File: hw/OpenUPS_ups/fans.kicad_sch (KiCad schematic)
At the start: 9 parts, among them J601 0022053031, J602 0022053031, Q601 2N7002, Q602 2N7002

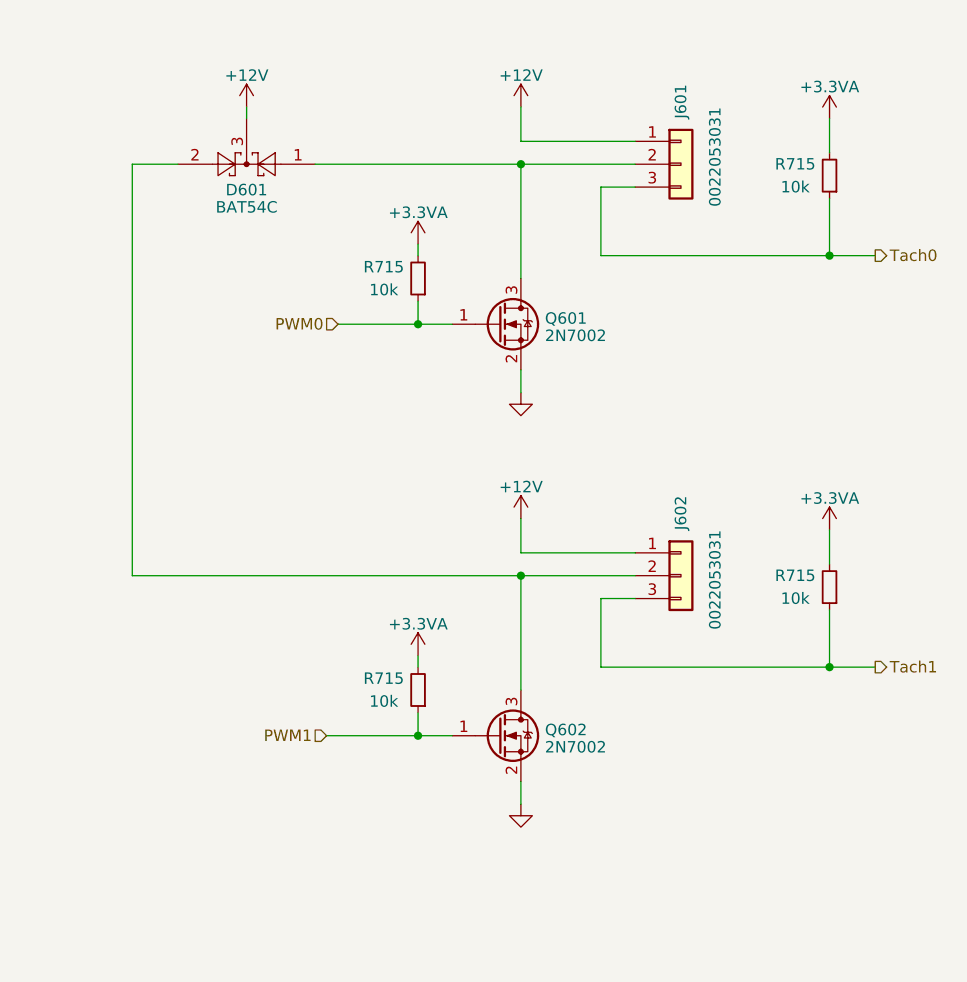
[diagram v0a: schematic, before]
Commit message: Added ports and fuses
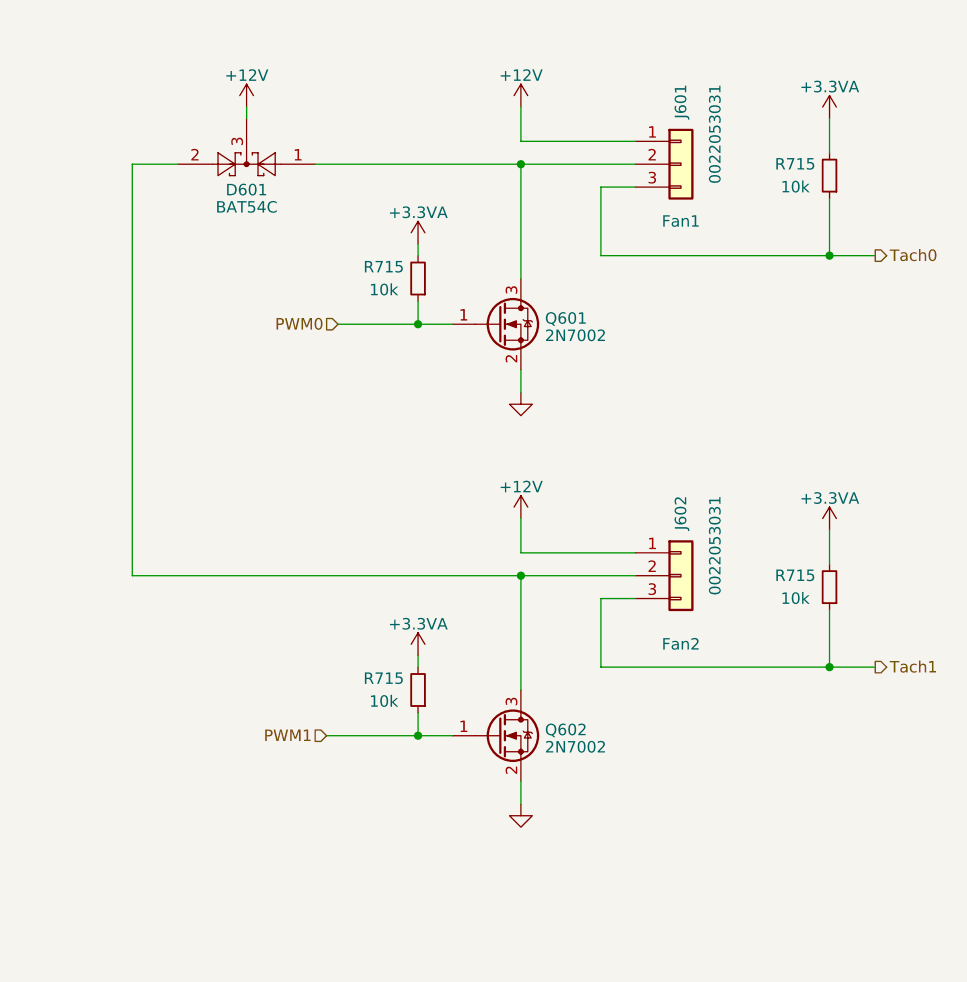
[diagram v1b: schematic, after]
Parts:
- J601: Label (none) -> Fan1
- J602: Label (none) -> Fan2
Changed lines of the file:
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@@
       (effects (font (size 1.27 1.27)) (justify right))
     )
-    (property "Value" "0022053031" (at 114.3 78.74 90)
+    (property "Value" "0022053031" (at 114.3 76.2 90)
       (effects (font (size 1.27 1.27)) (justify right))
     )
@@
     (property "Datasheet" "https://www.molex.com/pdm_docs/sd/022053031_sd.pdf" (at 110.49 85.09 0)
       (effects (font (size 1.27 1.27)) hide)
+    )
+    (property "Label" "Fan1" (at 110.49 91.44 0)
+      (effects (font (size 1.27 1.27)))
     )
     (pin "1")
@@
       (effects (font (size 1.27 1.27)) (justify right))
     )
-    (property "Value" "0022053031" (at 114.3 125.73 90)
+    (property "Value" "0022053031" (at 114.3 121.92 90)
       (effects (font (size 1.27 1.27)) (justify right))
     )
@@
       (effects (font (size 1.27 1.27)) hide)
     )
-    (pin "1")
+    (property "Label" "Fan2" (at 110.49 138.43 0)
+      (effects (font (size 1.27 1.27)))
+    )
+    (pin "1")

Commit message: Initial placement effort
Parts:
- renumbered D601 to D701, J601 to J701, J602 to J702, Q601 to Q701, Q602 to Q702
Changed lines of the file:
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@@
         )
         (path "/f77faec3-eac4-47f3-a2de-ec4a039f4502/4e3a8bef-51a9-4147-914d-0da741181736"
-          (reference "#PWR0608") (unit 1)
+          (reference "#PWR0702") (unit 1)
         )
       )
@@
         )
         (path "/f77faec3-eac4-47f3-a2de-ec4a039f4502/4e3a8bef-51a9-4147-914d-0da741181736"
-          (reference "#PWR0604") (unit 1)
+          (reference "#PWR0704") (unit 1)
         )
       )
@@
   (symbol (lib_id "Transistor_FET:2N7002") (at 90.17 102.87 0) (unit 1)
     (in_bom yes) (on_board yes) (dnp no) (fields_autoplaced)
-    (property "Reference" "Q601" (at 95.377 102.2263 0)
+    (property "Reference" "Q701" (at 95.377 102.2263 0)
       (effects (font (size 1.27 1.27)) (justify left))
     )
@@
       (project "OpenUPS_ups"
         (path "/f77faec3-eac4-47f3-a2de-ec4a039f4502/4e3a8bef-51a9-4147-914d-0da741181736"
-          (reference "Q601") (unit 1)
+          (reference "Q701") (unit 1)
         )
       )
@@
         )
         (path "/f77faec3-eac4-47f3-a2de-ec4a039f4502/4e3a8bef-51a9-4147-914d-0da741181736"
-          (reference "#PWR0607") (unit 1)
+          (reference "#PWR0708") (unit 1)
         )
       )
@@
         )
         (path "/f77faec3-eac4-47f3-a2de-ec4a039f4502/4e3a8bef-51a9-4147-914d-0da741181736"
-          (reference "#PWR0601") (unit 1)
+          (reference "#PWR0705") (unit 1)
         )
       )
@@
   (symbol (lib_id "Connector_Generic:Conn_01x03") (at 110.49 85.09 0) (unit 1)
     (in_bom yes) (on_board yes) (dnp no)
-    (property "Reference" "J601" (at 110.49 76.2 90)
+    (property "Reference" "J701" (at 110.49 76.2 90)
       (effects (font (size 1.27 1.27)) (justify right))
     )
@@
       (project "OpenUPS_ups"
         (path "/f77faec3-eac4-47f3-a2de-ec4a039f4502/4e3a8bef-51a9-4147-914d-0da741181736"
-          (reference "J601") (unit 1)
+          (reference "J701") (unit 1)
         )
       )
@@
         )
         (path "/f77faec3-eac4-47f3-a2de-ec4a039f4502/4e3a8bef-51a9-4147-914d-0da741181736"
-          (reference "#PWR0603") (unit 1)
+          (reference "#PWR0701") (unit 1)
         )
       )
@@
         )
         (path "/f77faec3-eac4-47f3-a2de-ec4a039f4502/4e3a8bef-51a9-4147-914d-0da741181736"
-          (reference "#PWR0605") (unit 1)
+          (reference "#PWR0706") (unit 1)
         )
       )
@@
         )
         (path "/f77faec3-eac4-47f3-a2de-ec4a039f4502/4e3a8bef-51a9-4147-914d-0da741181736"
-          (reference "#PWR0609") (unit 1)
+          (reference "#PWR0703") (unit 1)
         )
       )
@@
   (symbol (lib_id "Transistor_FET:2N7002") (at 90.17 148.59 0) (unit 1)
     (in_bom yes) (on_board yes) (dnp no) (fields_autoplaced)
-    (property "Reference" "Q602" (at 95.377 147.9463 0)
+    (property "Reference" "Q702" (at 95.377 147.9463 0)
       (effects (font (size 1.27 1.27)) (justify left))
     )
@@
       (project "OpenUPS_ups"
         (path "/f77faec3-eac4-47f3-a2de-ec4a039f4502/4e3a8bef-51a9-4147-914d-0da741181736"
-          (reference "Q602") (unit 1)
+          (reference "Q702") (unit 1)
         )
       )
@@
         )
         (path "/f77faec3-eac4-47f3-a2de-ec4a039f4502/4e3a8bef-51a9-4147-914d-0da741181736"
-          (reference "#PWR0602") (unit 1)
+          (reference "#PWR0709") (unit 1)
         )
       )
@@
   (symbol (lib_id "Diode:BAT54C") (at 62.23 85.09 180) (unit 1)
     (in_bom yes) (on_board yes) (dnp no) (fields_autoplaced)
-    (property "Reference" "D601" (at 62.23 87.9555 0)
+    (property "Reference" "D701" (at 62.23 87.9555 0)
       (effects (font (size 1.27 1.27)))
     )
@@
       (project "OpenUPS_ups"
         (path "/f77faec3-eac4-47f3-a2de-ec4a039f4502/4e3a8bef-51a9-4147-914d-0da741181736"
-          (reference "D601") (unit 1)
+          (reference "D701") (unit 1)
         )
       )
@@
         )
         (path "/f77faec3-eac4-47f3-a2de-ec4a039f4502/4e3a8bef-51a9-4147-914d-0da741181736"
-          (reference "R513") (unit 1)
+          (reference "R701") (unit 1)
         )
       )
@@
         )
         (path "/f77faec3-eac4-47f3-a2de-ec4a039f4502/4e3a8bef-51a9-4147-914d-0da741181736"
-          (reference "#PWR0606") (unit 1)
+          (reference "#PWR0707") (unit 1)
         )
       )
@@
         )
         (path "/f77faec3-eac4-47f3-a2de-ec4a039f4502/4e3a8bef-51a9-4147-914d-0da741181736"
-          (reference "R601") (unit 1)
+          (reference "R703") (unit 1)
         )
       )
@@
   (symbol (lib_id "Connector_Generic:Conn_01x03") (at 110.49 130.81 0) (unit 1)
     (in_bom yes) (on_board yes) (dnp no)
-    (property "Reference" "J602" (at 110.49 121.92 90)
+    (property "Reference" "J702" (at 110.49 121.92 90)
       (effects (font (size 1.27 1.27)) (justify right))
     )
@@
       (project "OpenUPS_ups"
         (path "/f77faec3-eac4-47f3-a2de-ec4a039f4502/4e3a8bef-51a9-4147-914d-0da741181736"
-          (reference "J602") (unit 1)
+          (reference "J702") (unit 1)
         )
       )
@@
         )
         (path "/f77faec3-eac4-47f3-a2de-ec4a039f4502/4e3a8bef-51a9-4147-914d-0da741181736"
-          (reference "R602") (unit 1)
+          (reference "R704") (unit 1)
         )
       )
@@
         )
         (path "/f77faec3-eac4-47f3-a2de-ec4a039f4502/4e3a8bef-51a9-4147-914d-0da741181736"
-          (reference "R514") (unit 1)
-        )
-      )
+          (reference "R702") (unit 1)
+        )
+      )

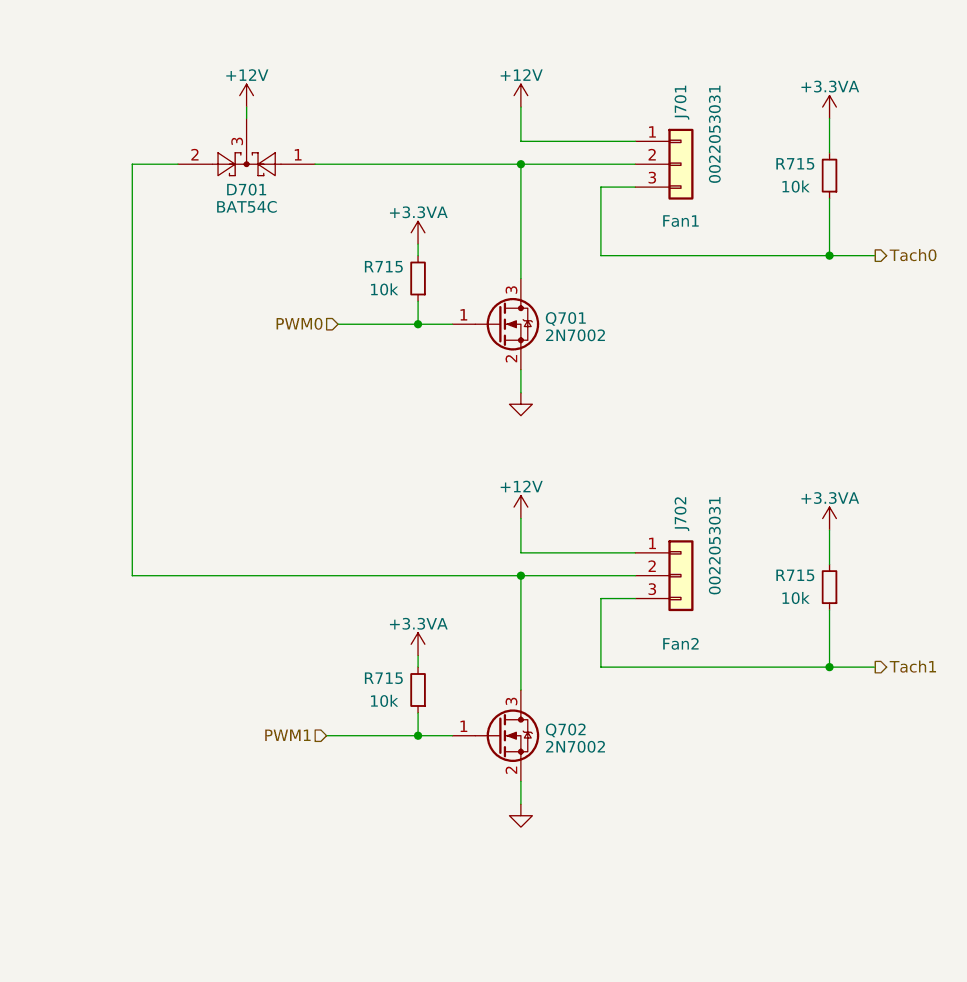
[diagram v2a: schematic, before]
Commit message: Issue #22 ESD protection on USB, Bat Data, Fans
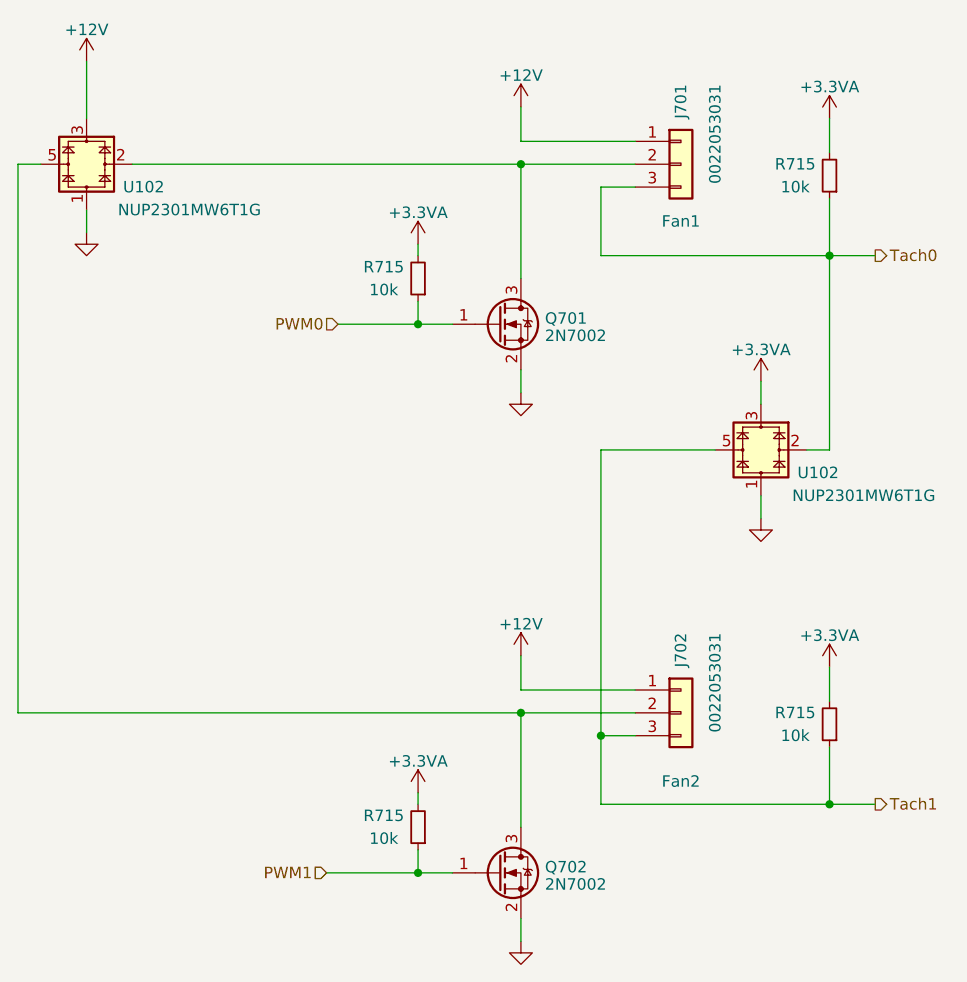
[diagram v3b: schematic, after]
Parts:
- removed D701: BAT54C, Package_TO_SOT_SMD:SOT-23, symbol Diode:BAT54C
- added U102 (x2): NUP2301MW6T1G, Package_TO_SOT_SMD:SOT-363_SC-70-6, symbol OpenUPS_ups:NUP2301MW6T1G
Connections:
- net +12V: now also U102.3
- net +3.3VA: now also U102.3
- net GND: now also U102.1, U102.1
- net Tach0: now also U102.2
- net Tach1: now also U102.5
- net at J701.2 (Pin_2), Q701.3 (D): now also U102.2
- net at J702.2 (Pin_2), Q702.3 (D): now also U102.5
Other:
- moved on the sheet: J702, Q702, R715
